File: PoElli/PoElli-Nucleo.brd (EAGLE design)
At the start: 120 parts, among them CN10 NUCLEO-CN10, CN7 NUCLEO-CN7, J3 M022.54MM, J4 M022.54MM, Q3 FDMC2674, Q4 IRFL4310, SW1 A6H2101, SW2 A6H2101, T1 Coilcraft 230NL, T2 FLYBACK750311689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

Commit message: routing draft v0.2, planes & routes in, optimization to be done..
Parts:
- moved C47 29.2 mm to (26.0, 11.2), turned to 270 degrees
- moved C46 26.9 mm to (28.2, 11.2), turned to 270 degrees
- moved C4 25.3 mm to (28.8, 42.6), turned to 180 degrees
- moved C44 22.3 mm to (31.3, 11.7)
- moved C43 22.3 mm to (31.2, 9.70)
- moved C45 22.2 mm to (31.3, 13.8)
- moved R5 20.6 mm to (57.3, 59.6)
- moved C9 15.9 mm to (12.5, 42.1)
- moved C15 11.7 mm to (31.2, 45.1)
- moved C2 10.7 mm to (22.6, 35.9)
- moved C1 10.3 mm to (16.3, 34.1)
- moved D4 10.2 mm to (35.9, 11.8), turned to 270 degrees
- moved R32 9.09 mm to (45.5, 15.3), turned to 180 degrees
- moved C6 8.32 mm to (28.8, 41.7), turned to 180 degrees
- moved C23 7.82 mm to (25.4, 17.2)
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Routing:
- net ETH_INT: track 0.00 -> 75.6 mm, vias 0 -> 3
- net POE_B+: track 0.00 -> 63.4 mm, vias 0 -> 3
- net ETH_SCK: track 0.00 -> 61.0 mm, vias 0 -> 2
- net ETH_MOSI: track 0.00 -> 54.6 mm
- net ETH_MISO: track 0.00 -> 54.6 mm, vias 0 -> 2
- net ETH_SS: track 0.00 -> 51.3 mm, vias 0 -> 3
- net POE_A+: track 0.00 -> 50.6 mm, vias 0 -> 2
- net N$2: track 0.00 -> 49.0 mm, vias 0 -> 2
- net POE_B-: track 0.00 -> 46.2 mm, vias 0 -> 2
- net TPOUT+: track 0.00 -> 45.4 mm, vias 0 -> 2
- net N$54: track 0.00 -> 45.3 mm, vias 0 -> 2
- net N$1: track 0.00 -> 44.2 mm, vias 0 -> 2
- net TPOUT-: track 0.00 -> 42.3 mm, vias 0 -> 2
- net POE_A-: track 0.00 -> 40.5 mm, vias 0 -> 2
- net UNREG_6V+: track 0.00 -> 39.5 mm, vias 0 -> 2
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- added copper zone on layer 15, net +3V3
- added copper zone on layer 15, net ENC-3V3
- added copper zone on layer 1, net GNDA
- added copper zone on layer 2, net GNDA
- added copper zone on layer 1, net RTN
- added copper zone on layer 2, net RTN
- added copper zone on layer 15, net VDD
- added copper zone on layer 15, net VIN
- added copper zone on layer 1, net VSS
- added copper zone on layer 2, net VSS
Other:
- board outline added: 79.5 x 70 mm

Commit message: gnd vias, planes etc
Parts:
- moved FB3 1.84 mm to (40.1, 42.7), turned to 270 degrees
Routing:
- net VSS: track 6.67 -> 0.00 mm, vias 1 -> 17
- net N$54: track 45.3 -> 49.5 mm
- net N$8: track 29.4 -> 31.1 mm
- net ETH_INT: track 75.6 -> 74.2 mm
- net POE_B-: track 46.2 -> 47.2 mm
- added copper zone on layer 16, net GNDA
- added copper zone on layer 16, net RTN
- added copper zone on layer 16, net VSS

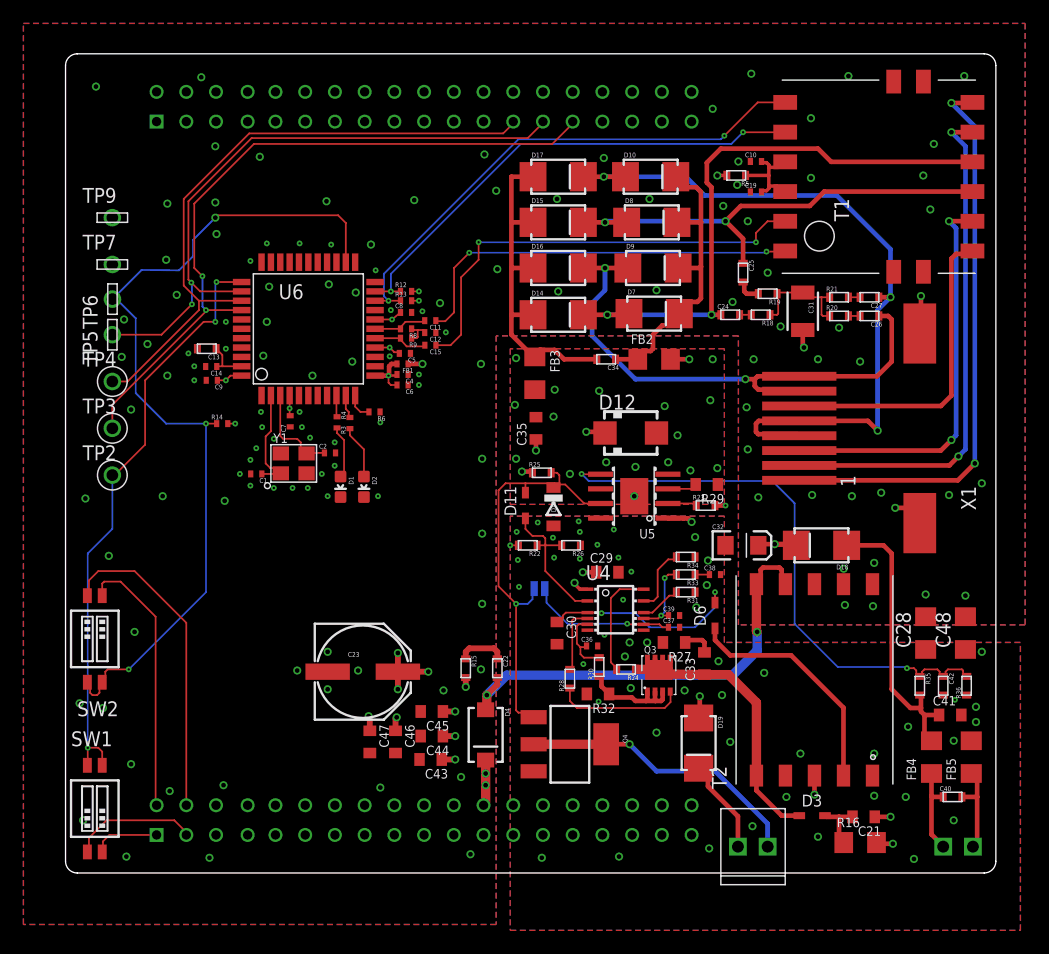
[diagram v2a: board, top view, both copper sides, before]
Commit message: smallest via drill to 0.25mm (was 0.2), + small improvments
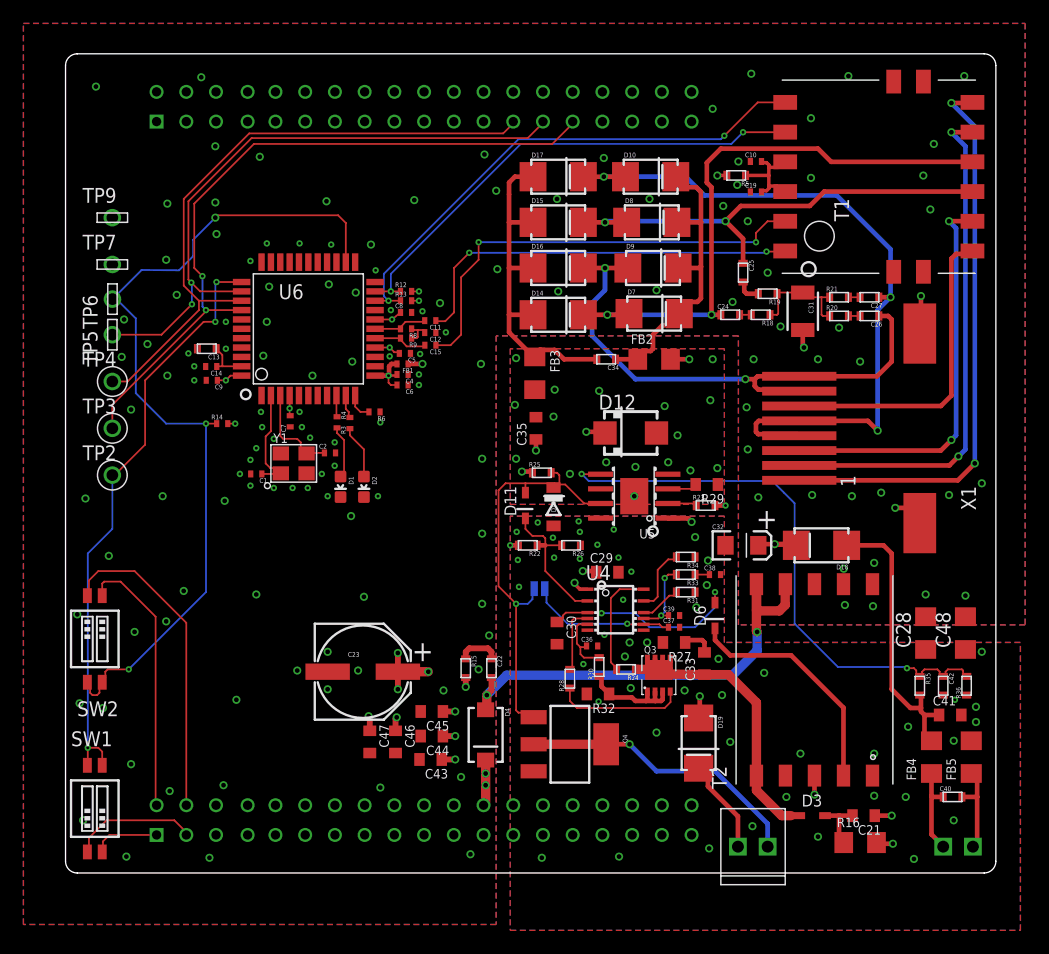
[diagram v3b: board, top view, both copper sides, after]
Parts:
- moved C22 0.50 mm to (36.4, 17.5)
- moved C21 0.10 mm to (68.2, 4.90)
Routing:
- net UNREG_6V+: track 39.5 -> 41.3 mm
- net N$8: track 31.1 -> 31.7 mm
- net N$16: track 4.15 -> 3.65 mm
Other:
- board text added: "+"

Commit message: review changes applied
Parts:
- added R10: 100, ELL-i-Passives:R0603
- added U$1: (no value), hapines:EH-LOGO
- C21: value 100nF -> 100nF 100V
- moved FB2 4.18 mm to (54.3, 42.7), turned to 270 degrees
- moved C21 2.20 mm to (70.4, 4.90)
- moved R29 1.90 mm to (54.8, 35.1), turned to 270 degrees
- moved C34 1.30 mm to (47.4, 44.4)
- moved R16 1.00 mm to (68.9, 2.60)
- moved C32 0.86 mm to (57.1, 28.5)
- moved R22 0.60 mm to (39.5, 27.4), turned to 270 degrees
- moved R34 0.30 mm to (52.7, 27.0)
- moved D12 0.20 mm to (48.3, 37.8)
- moved R27 0.10 mm to (52.1, 19.7)
- moved C10 0.10 mm to (59.0, 60.7)
- moved C19 0.10 mm to (59.0, 58.3)
- turned SW2 to 0 degrees
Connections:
- new net N$9: C21.2, R10.2
- net N$33: now also R10.1; no longer C21.2
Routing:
- net N$14: track 27.4 -> 15.6 mm
- net N$13: track 23.1 -> 14.2 mm
- net ETH_INT: track 74.2 -> 66.3 mm, vias 3 -> 2
- net N$6: track 26.5 -> 29.6 mm
- net POE_B-: track 47.2 -> 44.2 mm
- net N$19: track 2.53 -> 4.48 mm
- net U5_CDB: track 36.5 -> 35.1 mm
- net N$9: track 0.00 -> 1.15 mm
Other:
- board text added: ""PoElli-Nucleo" PoE shield proto"
- board text added: "ELL-i.org"
- board text added: "https://github.com/Ell-i/ELL-i-Eagle-Boards"

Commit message: final tweakings, draft v0.9
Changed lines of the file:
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@@
 <layer number="110" name="fp0" color="7" fill="1" visible="no" active="yes"/>
 <layer number="111" name="111" color="7" fill="1" visible="no" active="yes"/>
-<layer number="112" name="tSilk" color="7" fill="1" visible="no" active="yes"/>
-<layer number="113" name="bSilk" color="7" fill="1" visible="no" active="yes"/>
+<layer number="112" name="tSilk" color="7" fill="1" visible="yes" active="yes"/>
+<layer number="113" name="bSilk" color="7" fill="1" visible="yes" active="yes"/>
 <layer number="116" name="Patch_BOT" color="9" fill="4" visible="no" active="yes"/>
 <layer number="118" name="Rect_Pads" color="7" fill="1" visible="no" active="yes"/>
@@
 <contactref element="C48" pad="1"/>
 <polygon width="0.15" layer="16">
-<vertex x="81.6" y="19.7"/>
-<vertex x="56.3" y="19.7"/>
+<vertex x="81.6" y="19.8"/>
+<vertex x="56.3" y="19.8"/>
 <vertex x="56.3" y="30.5"/>
 <vertex x="38" y="30.5"/>
@@
 <via x="78.3" y="18.9" extent="1-16" drill="0.4"/>
 <polygon width="0.15" layer="1">
-<vertex x="81.6" y="19.7"/>
-<vertex x="56.3" y="19.7"/>
+<vertex x="81.6" y="19.8"/>
+<vertex x="56.3" y="19.8"/>
 <vertex x="56.3" y="30.5"/>
 <vertex x="38" y="30.5"/>
@@
 <via x="55.8" y="18.35" extent="1-16" drill="0.4"/>
 <polygon width="0.15" layer="2">
-<vertex x="81.6" y="19.7"/>
-<vertex x="56.3" y="19.7"/>
+<vertex x="81.6" y="19.8"/>
+<vertex x="56.3" y="19.8"/>
 <vertex x="56.3" y="30.5"/>
 <vertex x="38" y="30.5"/>
@@
 <via x="69" y="22.9" extent="1-16" drill="0.4"/>
 <via x="78.3" y="33.3" extent="1-16" drill="0.4"/>
-<via x="75.5" y="32.3" extent="1-16" drill="0.4"/>
+<via x="75.5" y="32.2" extent="1-16" drill="0.4"/>
 <via x="69.7" y="32.5" extent="1-16" drill="0.4"/>
 <via x="63.8" y="32.3" extent="1-16" drill="0.4"/>
@@
 <via x="63.1" y="44.9" extent="1-16" drill="0.4"/>
 <wire x1="63.1" y1="44.9" x2="70.9" y2="44.9" width="0.4" layer="2"/>
-<wire x1="70.9" y1="44.9" x2="73" y2="47" width="0.4" layer="2"/>
-<wire x1="73" y1="47" x2="73" y2="49.2" width="0.4" layer="2"/>
-<wire x1="73" y1="49.2" x2="73.1" y2="49.3" width="0.4" layer="2"/>
+<wire x1="70.9" y1="44.9" x2="73.1" y2="47.1" width="0.4" layer="2"/>
+<wire x1="73.1" y1="47.1" x2="73.1" y2="49.3" width="0.4" layer="2"/>
 <via x="73.1" y="49.3" extent="1-16" drill="0.4"/>
 <wire x1="73.1" y1="49.3" x2="73.1" y2="46.2" width="0.4" layer="1"/>
@@
 <contactref element="D19" pad="A"/>
 <polygon width="0.15" layer="15">
-<vertex x="39.8" y="-2"/>
-<vertex x="39.8" y="22.3"/>
-<vertex x="37.5" y="22.3"/>
-<vertex x="37.5" y="44.8"/>
+<vertex x="37.7" y="-1.9"/>
+<vertex x="37.7" y="44.8"/>
 <vertex x="84" y="44.8"/>
 <vertex x="84" y="-2"/>
@@
 <vertex x="28.2" y="-2.2"/>
 <vertex x="28.2" y="8.4"/>
-<vertex x="18.8" y="8.4"/>
-<vertex x="18.8" y="22.3"/>
-<vertex x="36.4" y="22.3"/>
-<vertex x="36.4" y="46"/>
+<vertex x="19.3" y="8.4"/>
+<vertex x="19.3" y="22.3"/>
+<vertex x="36.9" y="22.3"/>
+<vertex x="36.9" y="46"/>
 <vertex x="81.1" y="46"/>
 <vertex x="81.1" y="70.9"/>
 <vertex x="-2.3" y="70.9"/>
 <vertex x="-2.3" y="48.6"/>
-<vertex x="30.1" y="48.6"/>
-<vertex x="30.1" y="30.6"/>
-<vertex x="9.8" y="30.6"/>
-<vertex x="9.8" y="48.45"/>
-<vertex x="-2.3" y="48.45"/>
+<vertex x="29.9" y="48.6"/>
+<vertex x="29.9" y="30.6"/>
+<vertex x="10" y="30.6"/>
+<vertex x="10" y="48.5"/>
+<vertex x="-2.3" y="48.5"/>
 <vertex x="-2.3" y="-2.2"/>
 </polygon>
@@
 <contactref element="CN7" pad="24"/>
 <polygon width="0.15" layer="15">
-<vertex x="38.8" y="-2"/>
+<vertex x="36.9" y="-2"/>
 <vertex x="29.2" y="-2"/>
 <vertex x="29.2" y="9.4"/>
-<vertex x="19.7" y="9.4"/>
-<vertex x="19.7" y="21.3"/>
-<vertex x="38.8" y="21.3"/>
+<vertex x="20.1" y="9.4"/>
+<vertex x="20.1" y="21.5"/>
+<vertex x="36.9" y="21.5"/>
 </polygon>
 <via x="33.3" y="13.8" extent="1-16" drill="0.4"/>

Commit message: v1.0
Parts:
- moved TP9 0.70 mm to (4.00, 55.3)
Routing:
- added copper zone on layer 1, net N$199
- added copper zone on layer 15, net N$199
- added copper zone on layer 16, net N$199
- added copper zone on layer 2, net N$199
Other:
- board text added: "1"
- board text added: "2"
- board text added: "3"
- board text added: "4"
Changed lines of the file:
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@@
 <text x="68" y="61.2" size="1.778" layer="122" font="vector" ratio="15" rot="MR0">https://github.com/Ell-i/ELL-i-Eagle-Boards</text>
 <text x="8.8" y="61.8" size="1.5" layer="113" font="vector" ratio="15" rot="MR270">https://github.com/Ell-i/ELL-i-Eagle-Boards</text>
+<rectangle x1="29.7" y1="71.4" x2="42.7" y2="75.1" layer="41"/>
+<text x="3.6" y="57.4" size="2.54" layer="1" font="vector" ratio="20" rot="R90">1</text>
+<text x="3.5" y="60.3" size="2.54" layer="2" font="vector" ratio="20" rot="R90">2</text>
+<text x="3.6" y="63.6" size="2.54" layer="15" font="vector" ratio="20" rot="R90">3</text>
+<rectangle x1="29.7" y1="71.4" x2="42.7" y2="75.1" layer="42"/>
+<text x="3.6" y="66.6" size="2.54" layer="16" font="vector" ratio="20" rot="R90">4</text>
 </plain>
 <attributes>
@@
 <param name="mlMinCreamFrame" value="0mil"/>
 <param name="mlMaxCreamFrame" value="0mil"/>
-<param name="mlViaStopLimit" value="0mil"/>
+<param name="mlViaStopLimit" value="0.41mm"/>
 <param name="srRoundness" value="0"/>
 <param name="srMinRoundness" value="0mil"/>
@@
 <attribute name="VALUE" x="1.46" y="49.46" size="1.27" layer="21"/>
 </element>
-<element name="TP9" library="ELL-i-Passives" package="TP_5021" value="" x="4" y="56" smashed="yes">
-<attribute name="NAME" x="2.96" y="56.67" size="0.6096" layer="21" font="vector"/>
-<attribute name="VALUE" x="1.46" y="53.46" size="1.27" layer="21"/>
+<element name="TP9" library="ELL-i-Passives" package="TP_5021" value="" x="4" y="55.3" smashed="yes">
+<attribute name="NAME" x="2.96" y="55.97" size="0.6096" layer="21" font="vector"/>
+<attribute name="VALUE" x="1.46" y="52.76" size="1.27" layer="21"/>
 </element>
 <element name="SW1" library="SparkFun-Electromechanical" package="DIPSWITCH-02-50MIL" value="A6H2101" x="2.5" y="5.5" smashed="yes">
@@
 <via x="9.7" y="49.4" extent="1-16" drill="0.4"/>
 <via x="5" y="47.3" extent="1-16" drill="0.4"/>
-<via x="2.6" y="67.2" extent="1-16" drill="0.4"/>
+<via x="5.5" y="67" extent="1-16" drill="0.4"/>
 <via x="1.7" y="32" extent="1-16" drill="0.4"/>
 <via x="10" y="31.4" extent="1-16" drill="0.4"/>
@@
 <vertex x="81.1" y="70.9"/>
 <vertex x="-2.3" y="70.9"/>
-<vertex x="-2.3" y="48.6"/>
-<vertex x="29.9" y="48.6"/>
+<vertex x="-2.3" y="51.4"/>
+<vertex x="29.9" y="51.4"/>
 <vertex x="29.9" y="30.6"/>
 <vertex x="10" y="30.6"/>
-<vertex x="10" y="48.5"/>
-<vertex x="-2.3" y="48.5"/>
+<vertex x="10" y="51.3"/>
+<vertex x="-2.3" y="51.3"/>
 <vertex x="-2.3" y="-2.2"/>
 </polygon>
@@
 <vertex x="11.1" y="31.5"/>
 <vertex x="28.9" y="31.5"/>
-<vertex x="28.9" y="47.7"/>
-<vertex x="11.1" y="47.7"/>
+<vertex x="28.9" y="50.5"/>
+<vertex x="11.1" y="50.5"/>
 </polygon>
 <wire x1="28.625" y1="47.9" x2="27.9" y2="47.3" width="0.15" layer="1"/>
@@
 <wire x1="69.45" y1="4.9" x2="68.3" y2="4.9" width="0.4" layer="1"/>
 </signal>
+<signal name="N$199">
+<polygon width="0.2" layer="15" pour="cutout">
+<vertex x="0.6" y="56.7"/>
+<vertex x="4.1" y="56.7"/>
+<vertex x="4.1" y="69.4"/>
+<vertex x="0.6" y="69.4"/>
+</polygon>
+<polygon width="0.2" layer="2" pour="cutout">
+<vertex x="0.6" y="56.7"/>
+<vertex x="4.1" y="56.7"/>
+<vertex x="4.1" y="69.4"/>
+<vertex x="0.6" y="69.4"/>
+</polygon>
+<polygon width="0.2" layer="16" pour="cutout">
+<vertex x="0.6" y="56.7"/>
+<vertex x="4.1" y="56.7"/>
+<vertex x="4.1" y="69.4"/>
+<vertex x="0.6" y="69.4"/>
+</polygon>
+<polygon width="0.2" layer="1" pour="cutout">
+<vertex x="0.6" y="56.7"/>
+<vertex x="4.1" y="56.7"/>
+<vertex x="4.1" y="69.4"/>
+<vertex x="0.6" y="69.4"/>
+</polygon>
+</signal>
 </signals>

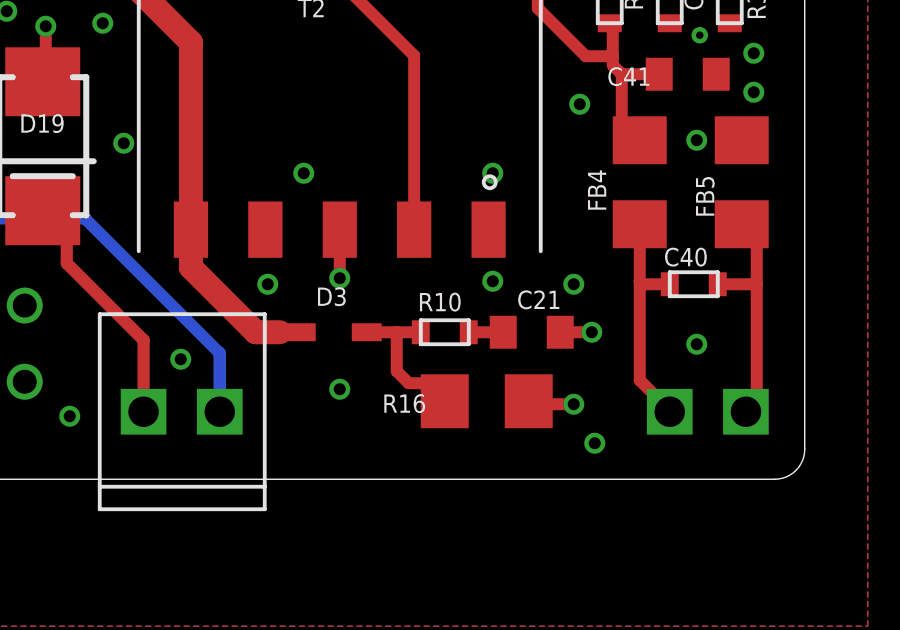
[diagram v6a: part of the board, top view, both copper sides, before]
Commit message: Add PoElli-Nucleo.brd to preserve backannotation
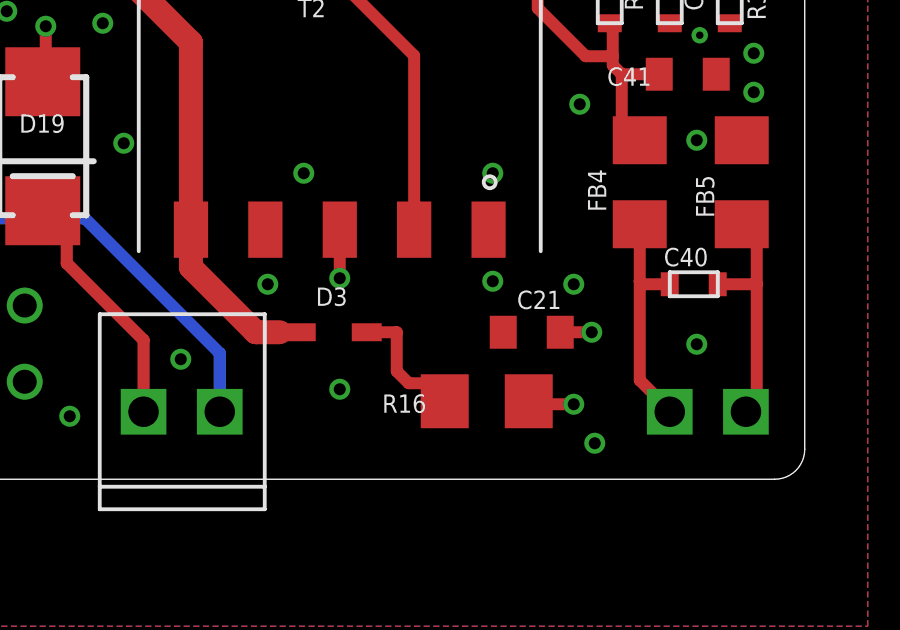
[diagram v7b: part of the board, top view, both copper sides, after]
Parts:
- removed R10: 100, ELL-i-Passives:R0603
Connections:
- net N$33: no longer R10.1
- net N$9: no longer R10.2
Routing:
- net N$9: track 1.15 -> 0.00 mm
- net N$33: track 5.15 -> 4.35 mm
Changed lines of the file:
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@@
 </element>
 <element name="U$1" library="hapines" package="EH-LOGO" value="" x="50.1" y="9.6" smashed="yes"/>
-<element name="R10" library="ELL-i-Passives" package="R0603" value="100" x="67.5" y="4.9" smashed="yes">
-<attribute name="NAME" x="66.6" y="5.6" size="0.6096" layer="25" font="vector"/>
-<attribute name="VALUE" x="66.4" y="4" size="0.4064" layer="27"/>
-</element>
 </elements>
 <signals>
@@
 <wire x1="66.3" y1="3.2" x2="65.9" y2="3.6" width="0.4" layer="1"/>
 <wire x1="65.9" y1="3.6" x2="65.9" y2="4.9" width="0.4" layer="1"/>
-<contactref element="R10" pad="1"/>
-<wire x1="65.9" y1="4.9" x2="66.7" y2="4.9" width="0.4" layer="1"/>
 </signal>
 <signal name="POE_A+" class="1">
@@
 <signal name="N$9">
 <contactref element="C21" pad="2"/>
-<contactref element="R10" pad="2"/>
-<wire x1="69.45" y1="4.9" x2="68.3" y2="4.9" width="0.4" layer="1"/>
 </signal>
 <signal name="N$199">

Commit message: Fix broken net between C21 and D3/R16
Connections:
- removed net N$9: C21.2
- net N$33: now also C21.2
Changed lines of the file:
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@@
 <wire x1="66.3" y1="3.2" x2="65.9" y2="3.6" width="0.4" layer="1"/>
 <wire x1="65.9" y1="3.6" x2="65.9" y2="4.9" width="0.4" layer="1"/>
+<contactref element="C21" pad="2"/>
+<wire x1="67" y1="3.2" x2="69.45" y2="4.9" width="0" layer="19" extent="1-1"/>
 </signal>
 <signal name="POE_A+" class="1">
@@
 <wire x1="3.135" y1="16.065" x2="3.135" y2="16.3" width="0.15" layer="1"/>
 </signal>
-<signal name="N$9">
-<contactref element="C21" pad="2"/>
-</signal>
 <signal name="N$199">
